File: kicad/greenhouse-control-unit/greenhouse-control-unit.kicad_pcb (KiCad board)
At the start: 2 copper layers, 71 parts, among them J1 Pluggable_Terminal_01x02, J10 Molex_KK-254_01x10, J10_LittleBuck1 Conn_01x01_Female, J11_LittleBuck1 Conn_01x01_Female, J12_BigBuck1 Conn_01x01_Female, J13_BigBuck1 Conn_01x01_Female, J14_LittleBuck1 Conn_01x01_Female, J15_LittleBuck1 Conn_01x01_Female, J2 Pluggable_Terminal_01x02, J3 Pluggable_Terminal_01x02, J4 Molex_KK-254_01x08, J5 Conn_01x10_Female, J6 Conn_01x10_Female, J6_BigBuck1 Conn_01x01_Female, J7 Conn_01x15_Female, J7_BigBuck1 Conn_01x01_Female, J8 Conn_01x15_Female, J9 Molex_KK-396_01x16, Q1 2N7000, Q10 IRLB8721PBF, Q11 IRLB8721PBF, Q12 2N7000, Q13 2N7000, Q2 2N7000, Q3 2N7000, Q4 IRLB8721PBF, Q5 IRLB8721PBF, Q6 IRLB8721PBF, Q7 IRLB8721PBF, Q8 IRLB8721PBF, Q9 IRLB8721PBF, U1 74HC595, U2 74HC595

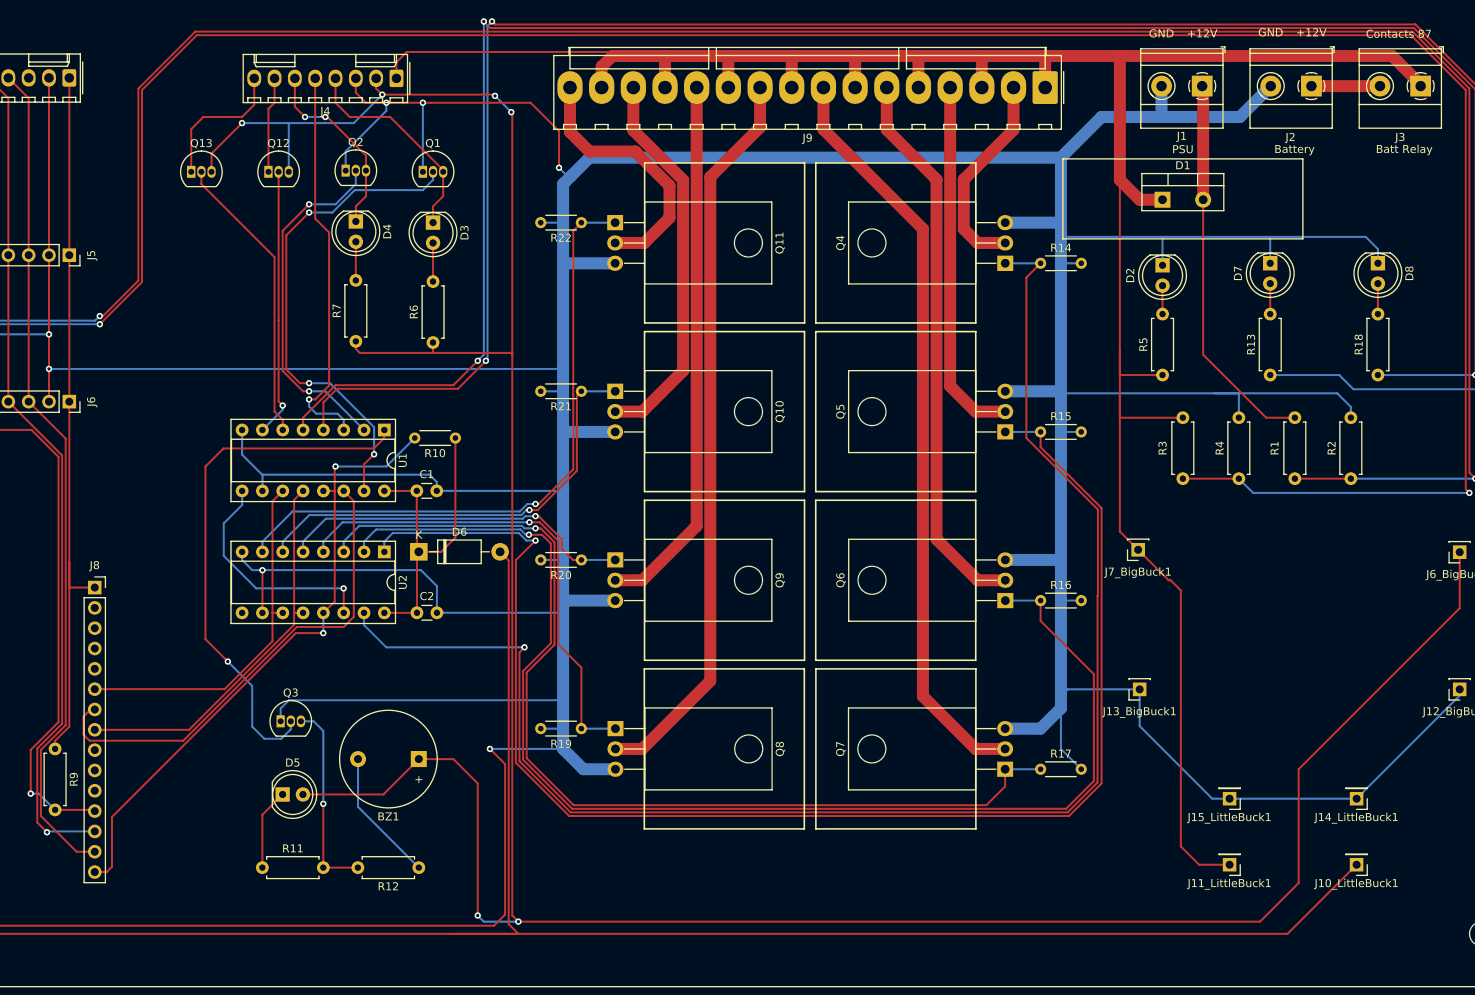
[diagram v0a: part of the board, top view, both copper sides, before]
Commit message: Moved 12V FET tracks to other side
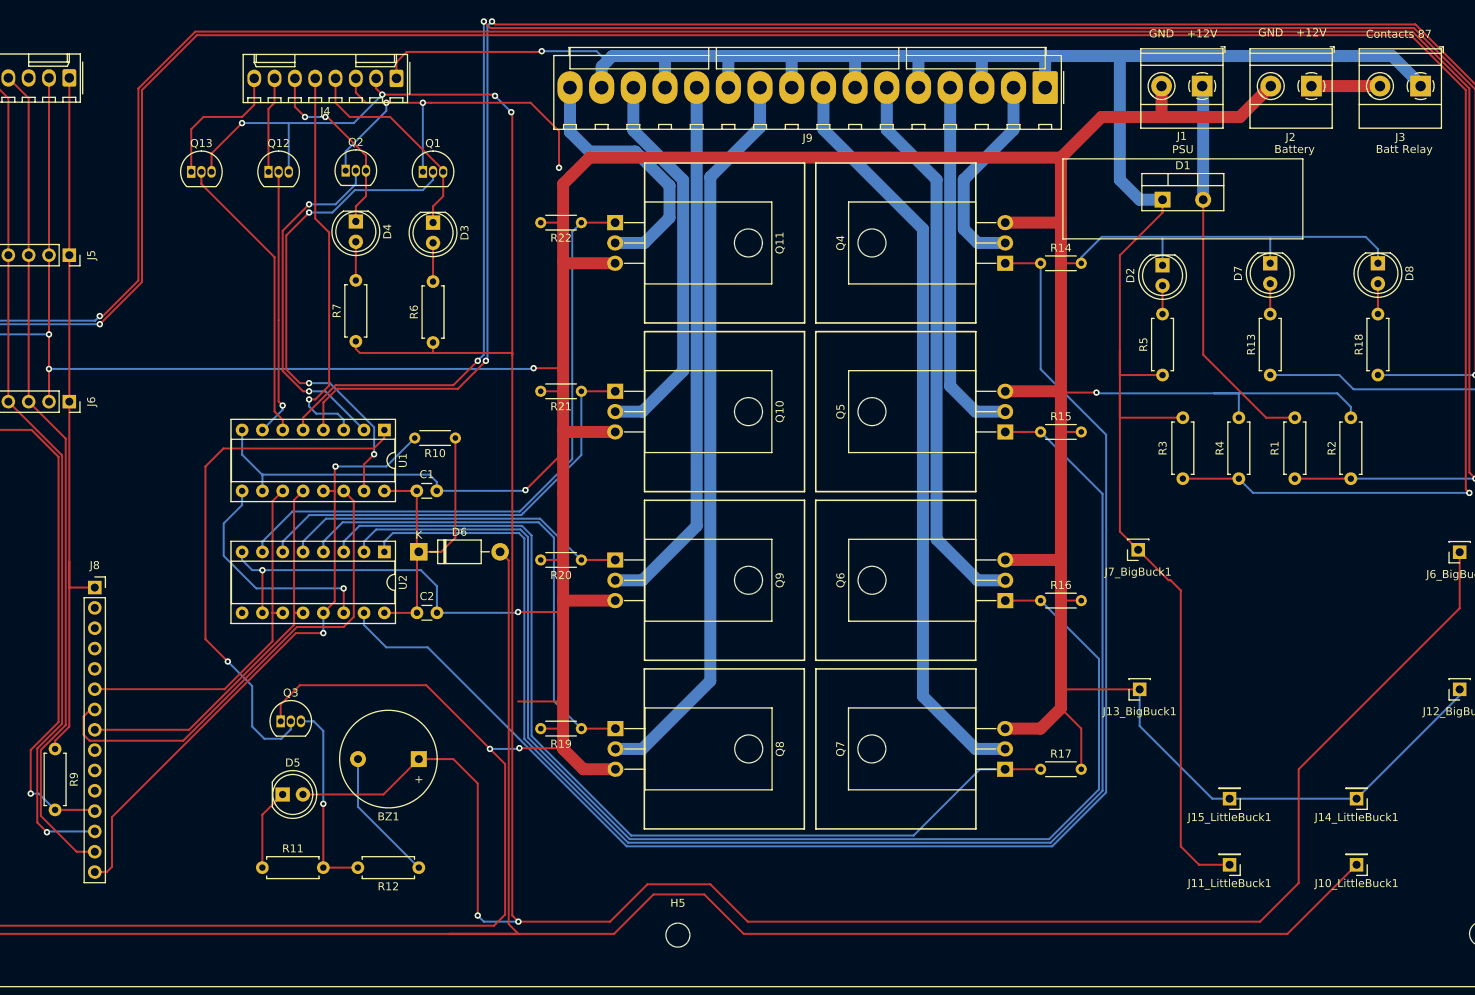
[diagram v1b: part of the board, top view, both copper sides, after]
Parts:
- added H5: MountingHole, MountingHole:MountingHole_3mm, F.Cu at (148.6, 150.9)
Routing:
- net /SW0_SR_Q08: track 187.5 -> 182.5 mm, vias 1 -> 0
- net /SW3_SR_Q11: track 127.5 -> 123.4 mm, vias 1 -> 0
- net +5VA: track 289.2 -> 293.3 mm
- net +5V: track 372.3 -> 376.1 mm
- net /SW1_SR_Q09: track 179.0 -> 177.4 mm, vias 1 -> 0
- net /SW2_SR_Q10: track 159.5 -> 158.1 mm, vias 1 -> 0
- net GND: track 930.8 -> 932.0 mm, vias 7 -> 12
- net /SW5_SR_Q13: track 44.6 -> 43.6 mm, vias 1 -> 0
- net /SW7_SR_Q15: track 79.4 -> 78.5 mm, vias 1 -> 0
- net /SW6_SR_Q14: track 56.1 -> 55.3 mm, vias 1 -> 0
- net +12V: track 299.8 -> 299.3 mm, vias 0 -> 1
- net /SW4_SR_Q12: vias 1 -> 0

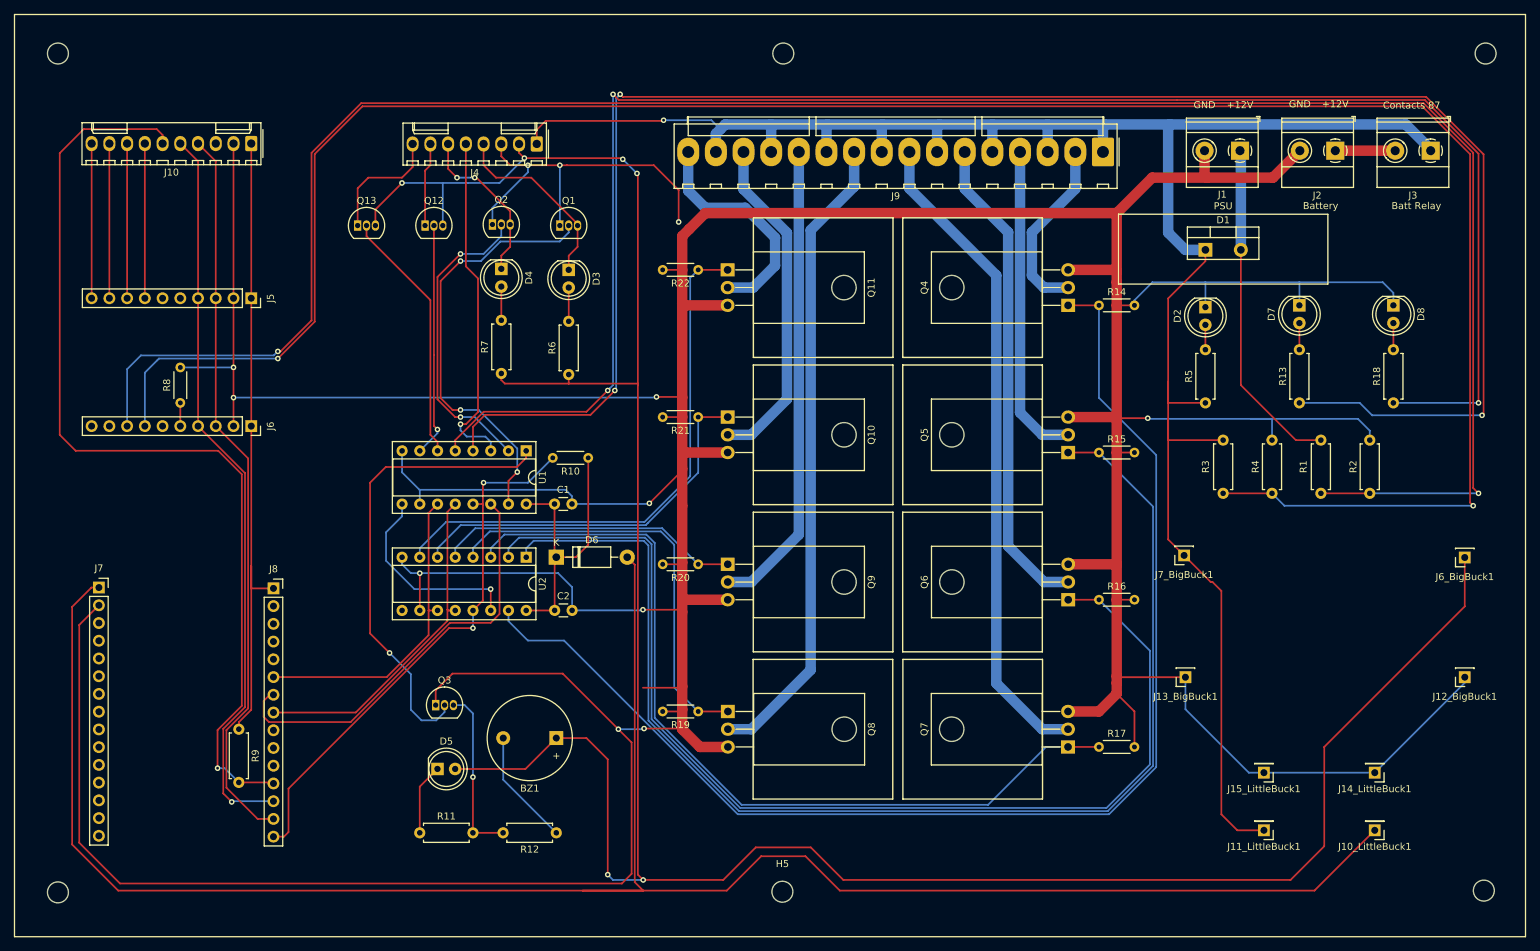
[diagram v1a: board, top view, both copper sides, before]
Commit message: Add ground plane
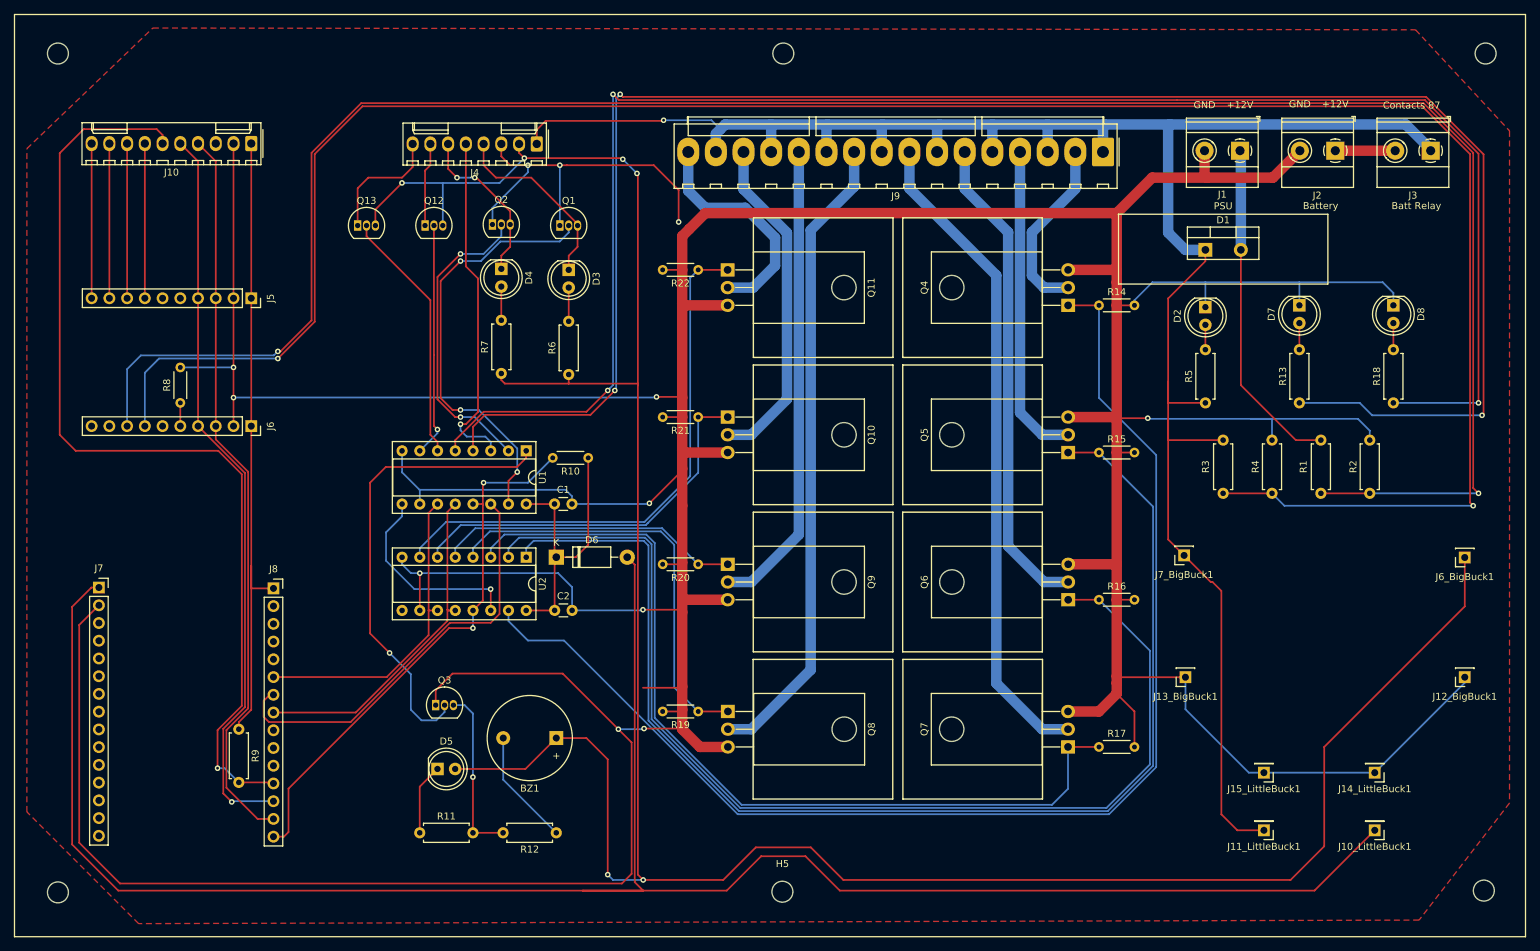
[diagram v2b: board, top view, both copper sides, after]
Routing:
- net /SW3_SR_Q11: track 123.4 -> 126.9 mm
- added copper zone on F.Cu, net GND
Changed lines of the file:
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@@
   (segment (start 201.22648 132.655802) (end 201.22648 116.355838) (width 0.25) (layer "B.Cu") (net 39))
   (segment (start 193.930642 130.142) (end 189.494856 130.142) (width 0.25) (layer "F.Cu") (net 40))
-  (segment (start 142.748 138.43) (end 178.054 138.43) (width 0.25) (layer "B.Cu") (net 40))
+  (segment (start 106.818642 101.704) (end 106.808642 101.694) (width 0.25) (layer "B.Cu") (net 40))
+  (segment (start 142.748 138.43) (end 187.198 138.43) (width 0.25) (layer "B.Cu") (net 40))
+  (segment (start 106.818642 102.974) (end 106.818642 101.704) (width 0.25) (layer "B.Cu") (net 40))
+  (segment (start 129.098863 99.72048) (end 130.302 100.923617) (width 0.25) (layer "B.Cu") (net 40))
+  (segment (start 130.302 125.984) (end 142.748 138.43) (width 0.25) (layer "B.Cu") (net 40))
+  (segment (start 106.808642 101.694) (end 108.782162 99.72048) (width 0.25) (layer "B.Cu") (net 40))
+  (segment (start 187.198 138.43) (end 189.494856 136.133144) (width 0.25) (layer "B.Cu") (net 40))
+  (segment (start 189.494856 136.133144) (end 189.494856 130.142) (width 0.25) (layer "B.Cu") (net 40))
   (segment (start 108.782162 99.72048) (end 129.098863 99.72048) (width 0.25) (layer "B.Cu") (net 40))
   (segment (start 130.302 100.923617) (end 130.302 125.984) (width 0.25) (layer "B.Cu") (net 40))
-  (segment (start 106.808642 101.694) (end 108.782162 99.72048) (width 0.25) (layer "B.Cu") (net 40))
-  (segment (start 130.302 125.984) (end 142.748 138.43) (width 0.25) (layer "B.Cu") (net 40))
-  (segment (start 186.342 130.142) (end 189.494856 130.142) (width 0.25) (layer "B.Cu") (net 40))
-  (segment (start 129.098863 99.72048) (end 130.302 100.923617) (width 0.25) (layer "B.Cu") (net 40))
-  (segment (start 178.054 138.43) (end 186.342 130.142) (width 0.25) (layer "B.Cu") (net 40))
-  (segment (start 106.818642 102.974) (end 106.818642 101.704) (width 0.25) (layer "B.Cu") (net 40))
-  (segment (start 106.818642 101.704) (end 106.808642 101.694) (width 0.25) (layer "B.Cu") (net 40))
   (segment (start 89.028642 56.99) (end 98.172642 66.134) (width 0.25) (layer "F.Cu") (net 41))
   (segment (start 98.172642 66.134) (end 98.172642 85.438) (width 0.25) (layer "F.Cu") (net 41))
@@
   (segment (start 101.738642 101.704) (end 101.728642 101.694) (width 0.25) (layer "B.Cu") (net 43))
   (segment (start 104.601202 98.82144) (end 131.368082 98.82144) (width 0.25) (layer "B.Cu") (net 43))
-  (segment (start 67.438642 84.193) (end 72.069122 88.82348) (width 0.25) (layer "F.Cu") (net 44))
+  (segment (start 68.962642 135.984) (end 73.430642 140.452) (width 0.25) (layer "F.Cu") (net 44))
   (segment (start 67.438642 46.266) (end 67.438642 65.88) (width 0.25) (layer "F.Cu") (net 44))
+  (segment (start 68.962642 127.728282) (end 68.962642 135.984) (width 0.25) (layer "F.Cu") (net 44))
   (segment (start 64.898642 43.726) (end 67.438642 46.266) (width 0.25) (layer "F.Cu") (net 44))
+  (segment (start 67.438642 84.193) (end 67.438642 86.097282) (width 0.25) (layer "F.Cu") (net 44))
   (segment (start 67.438642 65.88) (end 67.438642 84.193) (width 0.25) (layer "F.Cu") (net 44))
-  (segment (start 72.069122 88.82348) (end 72.069122 124.621802) (width 0.25) (layer "F.Cu") (net 44))
-  (segment (start 68.962642 127.728282) (end 68.962642 135.984) (width 0.25) (layer "F.Cu") (net 44))
-  (segment (start 68.962642 135.984) (end 73.430642 140.452) (width 0.25) (layer "F.Cu") (net 44))
+  (segment (start 67.438642 86.097282) (end 72.069122 90.727763) (width 0.25) (layer "F.Cu") (net 44))
+  (segment (start 72.069122 90.727763) (end 72.069122 124.621802) (width 0.25) (layer "F.Cu") (net 44))
   (segment (start 72.069122 124.621802) (end 68.962642 127.728282) (width 0.25) (layer "F.Cu") (net 44))
   (segment (start 73.430642 140.452) (end 75.699642 140.452) (width 0.25) (layer "F.Cu") (net 44))
@@
   (via (at 101.982642 48.608) (size 0.8) (drill 0.4) (layers "F.Cu" "B.Cu") (net 86))
   (segment (start 101.982642 48.608) (end 104.522642 48.608) (width 0.25) (layer "B.Cu") (net 86))
+  (zone (net 0) (net_name "") (layer "F.Cu") (hatch edge 0.508)
+    (connect_pads (clearance 0))
+    (min_thickness 0.254)
+    (keepout (tracks allowed) (vias allowed) (pads allowed ) (copperpour not_allowed) (footprints allowed))
+    (fill (thermal_gap 0.508) (thermal_bridge_width 0.508))
+    (polygon
+      (pts
+        (xy 186.69 138.43)
+        (xy 143.764 138.43)
+        (xy 143.51 53.848)
+        (xy 186.69 53.848)
+      )
+    )
+  )
+  (zone (net 1) (net_name "GND") (layer "F.Cu") (hatch edge 0.508)
+    (connect_pads (clearance 0.508))
+    (min_thickness 0.254) (filled_areas_thickness no)
+    (fill yes (thermal_gap 0.508) (thermal_bridge_width 0.508))
+    (polygon
+      (pts
+        (xy 252.73 41.91)
+        (xy 252.73 138.176)
+        (xy 239.776 154.94)
+        (xy 56.388 155.448)
+        (xy 40.386 139.446)
+        (xy 40.386 44.45)
+        (xy 58.42 27.178)
+        (xy 239.268 27.432)
+      )
+    )
+  )
   (group "" (id 317c35b6-c437-4c26-9dfe-08151afaa9bd)
     (members

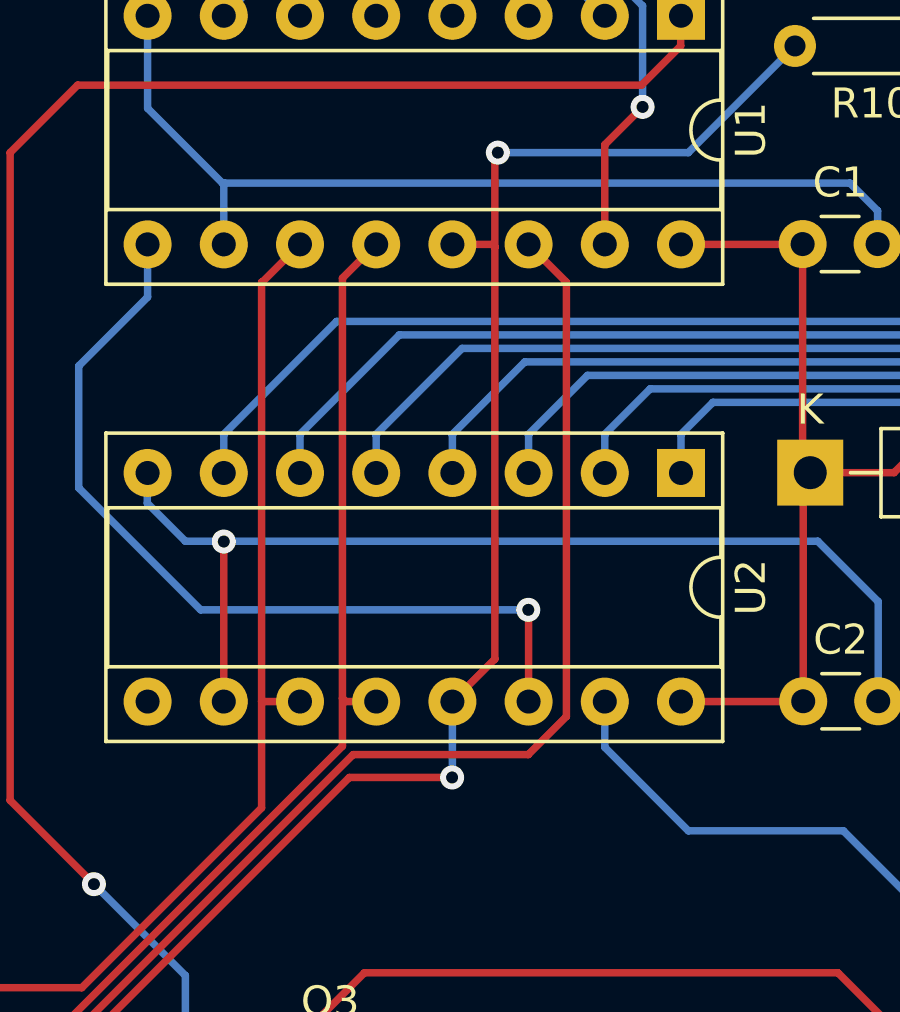
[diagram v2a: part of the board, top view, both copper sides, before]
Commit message: SRCLR on SR must be high
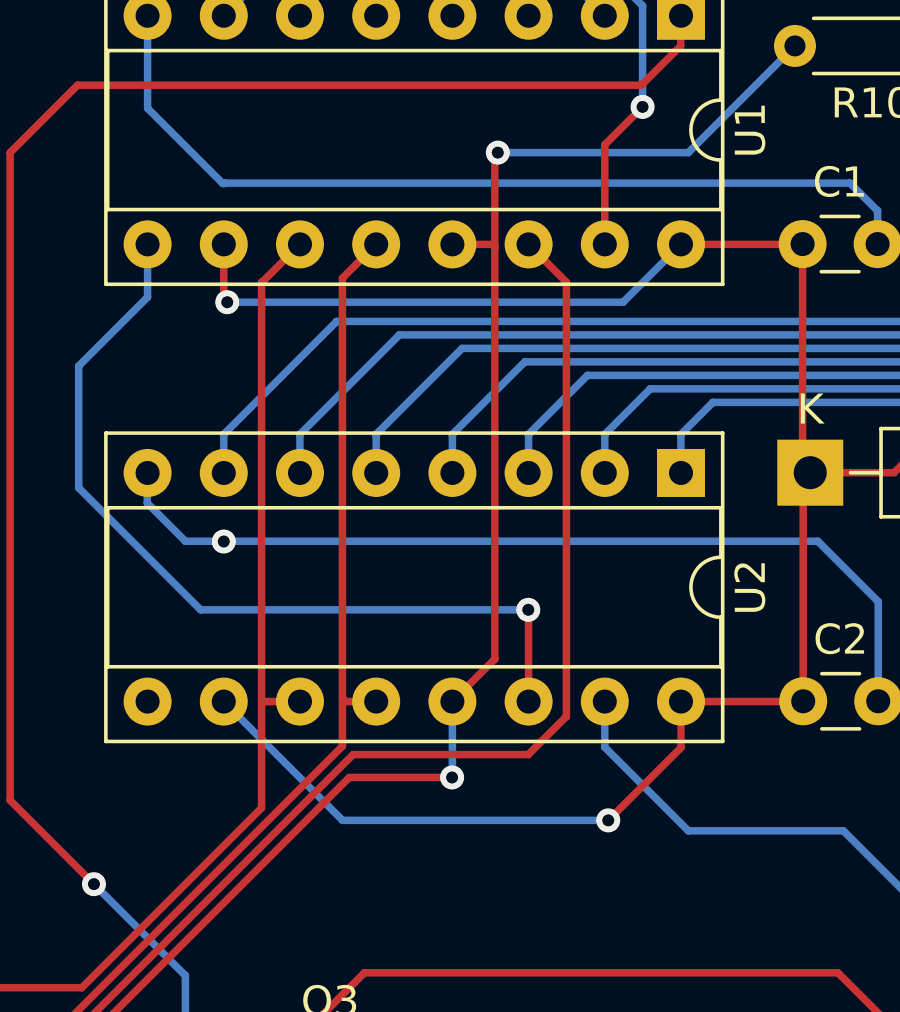
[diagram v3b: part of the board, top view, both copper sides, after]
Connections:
- J5 pad 5: /ADC1_ADDR -> GND
- J6 pad 5: /ADC2_ADDR -> /ADC1_SCA
- U1 pad 10: GND -> /SR_VCC
- U2 pad 10: GND -> /SR_VCC
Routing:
- net /SR_VCC: track 41.3 -> 78.7 mm, vias 0 -> 2
- net GND: track 932.0 -> 924.7 mm
- net /ADC1_SCA: track 105.9 -> 109.3 mm
- net /ADC2_ADDR: track 3.33 -> 0.00 mm
